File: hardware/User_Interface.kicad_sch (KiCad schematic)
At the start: 21 parts, among them J2 AYF531035, J3 Molex 5034800440, Q1 NMOS, Q2 NMOS

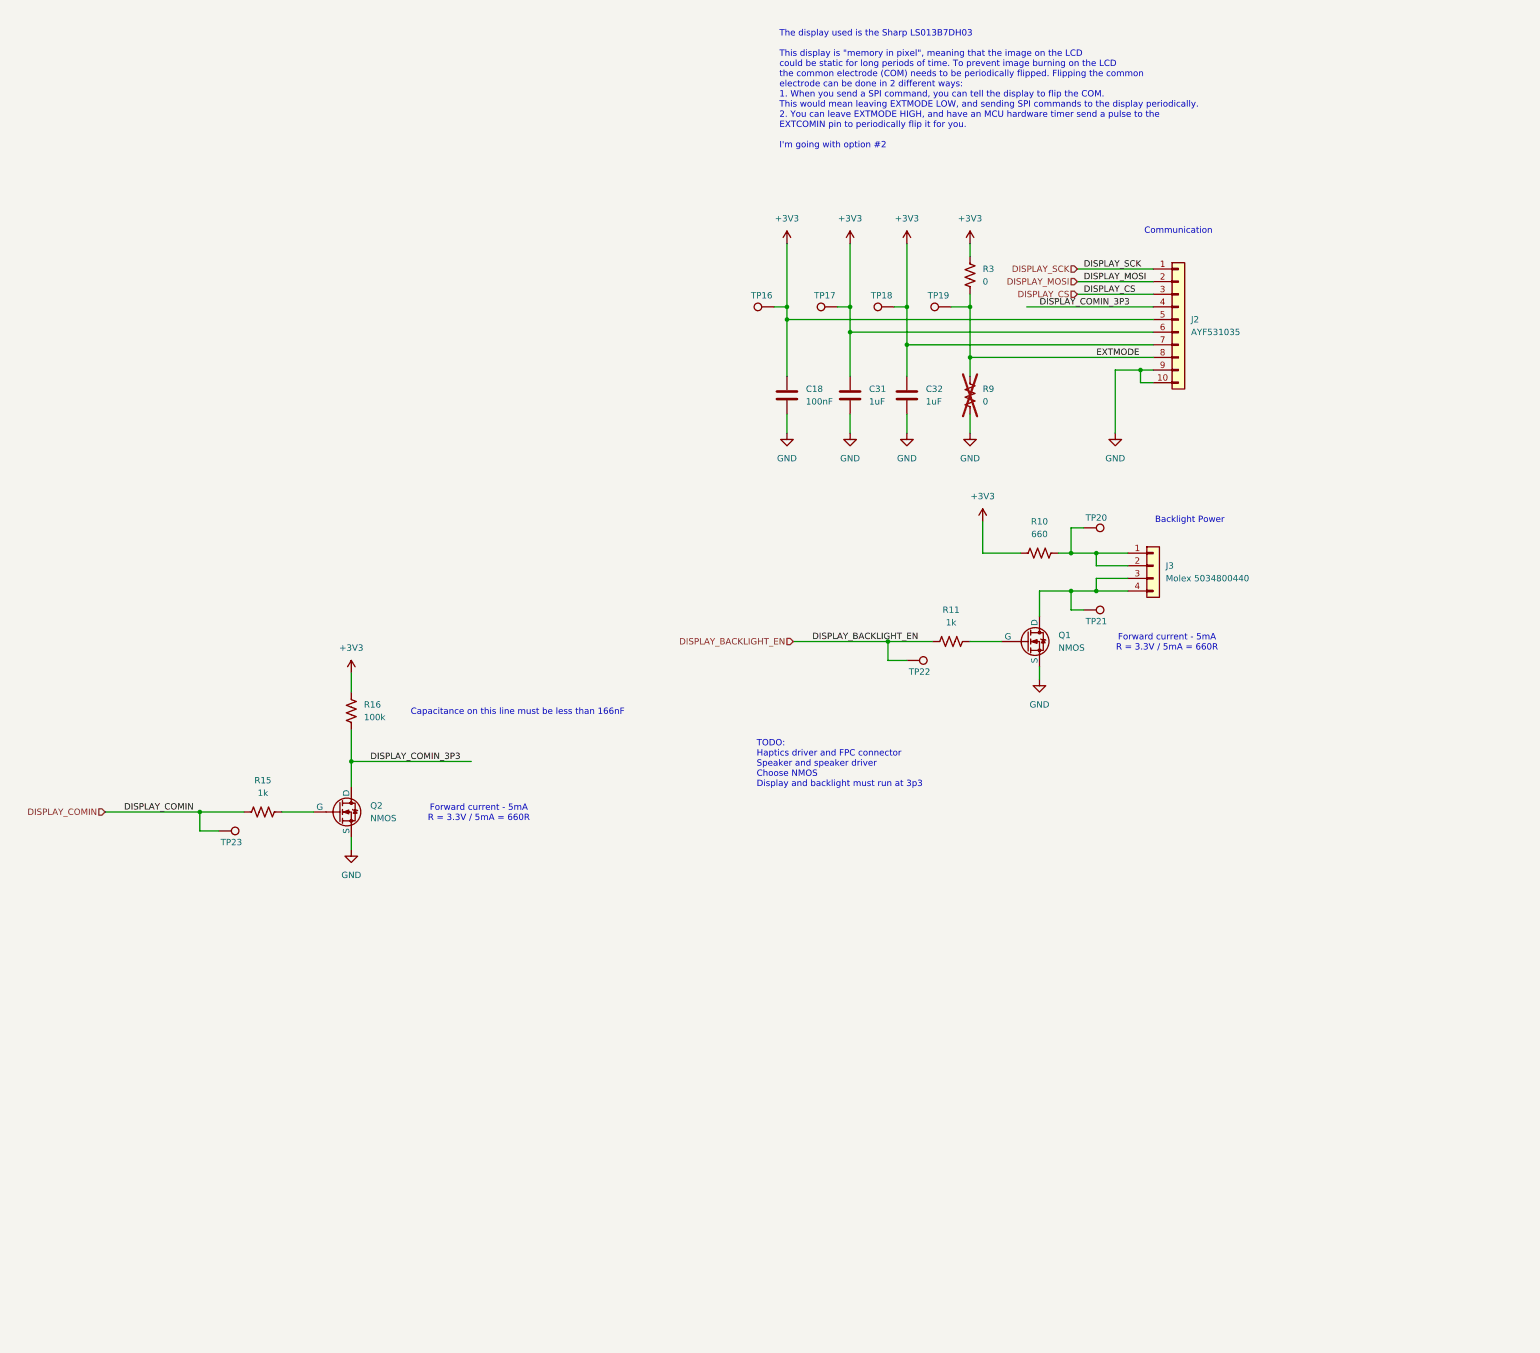
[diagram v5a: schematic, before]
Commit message: Added level translator, connected all misc GPIO. Ensured that 64QLFP has support for 1.8V
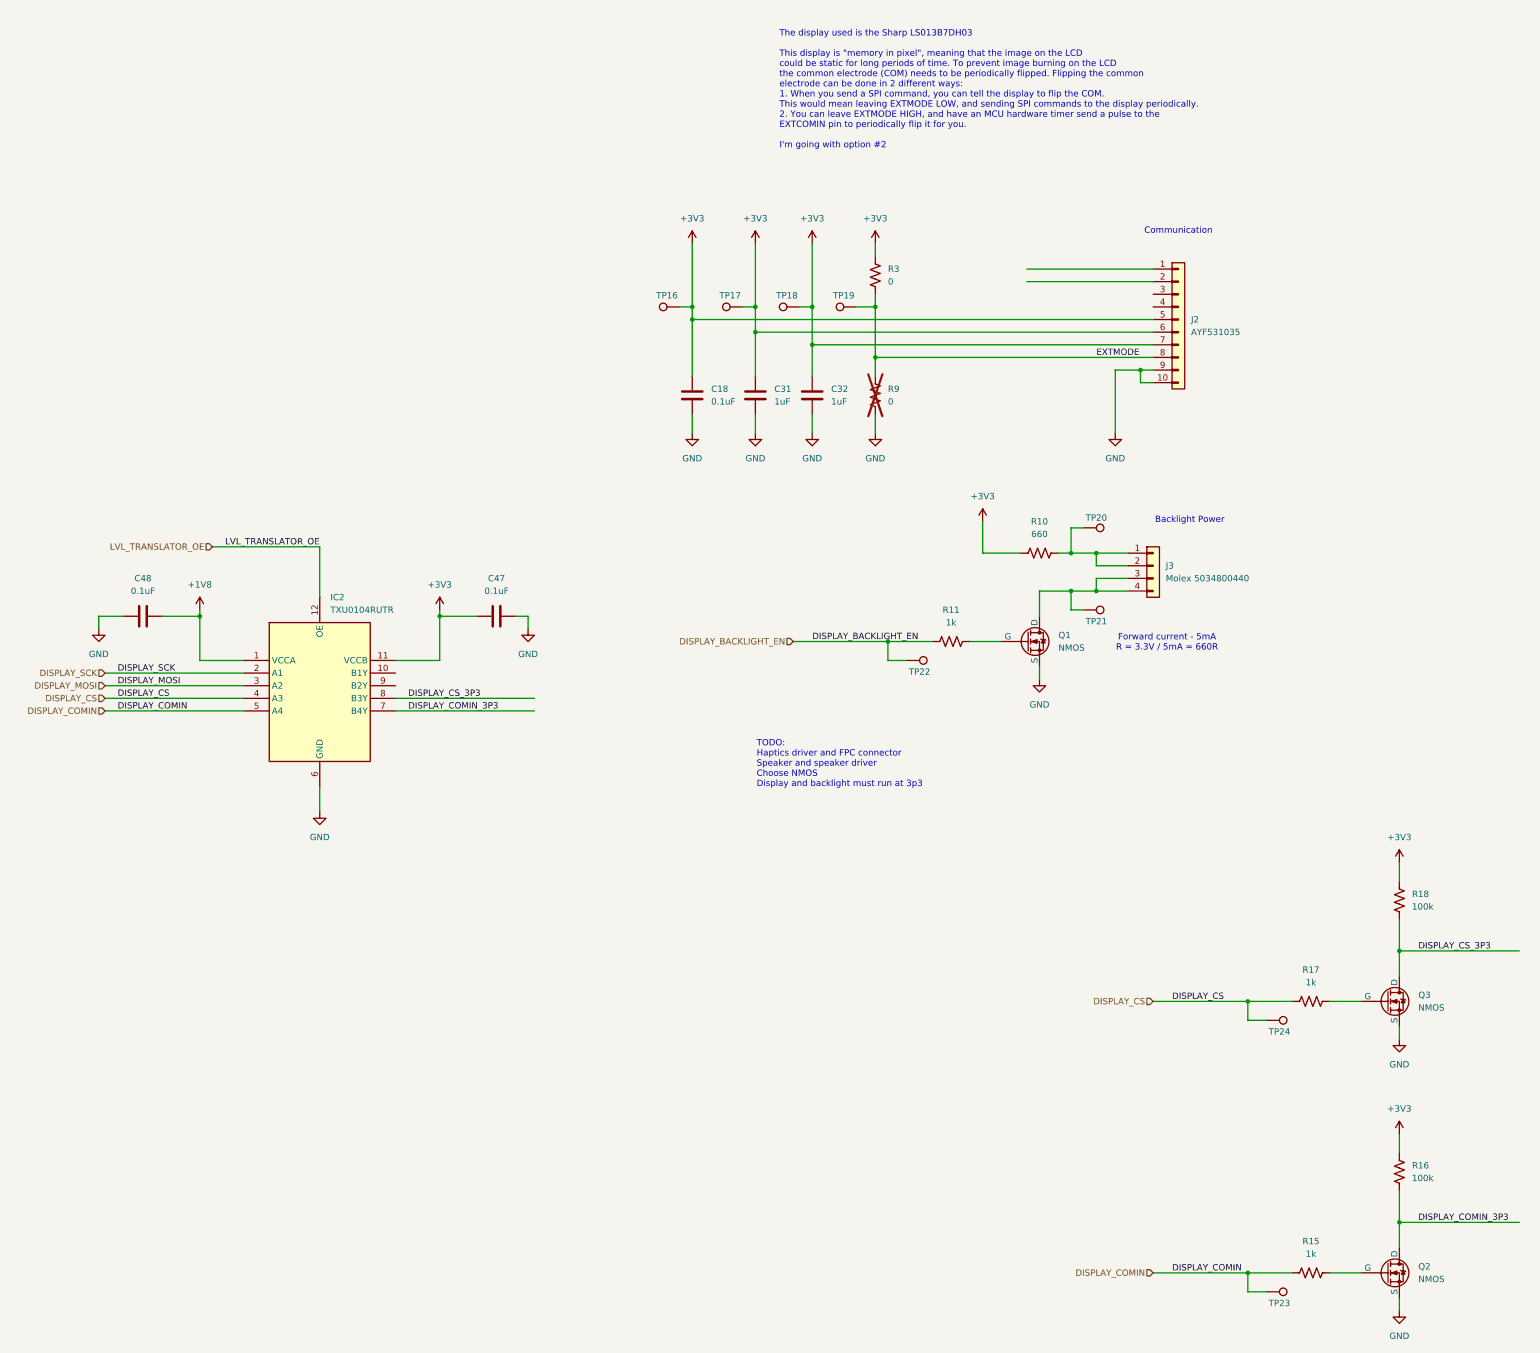
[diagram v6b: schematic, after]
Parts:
- added C47, C48: 0.1uF, symbol Device:C
- added IC2: TXU0104RUTR, TXU0104RUTR, symbol TXU0104RUTR:TXU0104RUTR
- added Q3: NMOS, symbol Simulation_SPICE:NMOS
- added R17: 1k, symbol Device:R_US
- added R18: 100k, symbol Device:R_US
- added TP24: TestPoint, symbol Connector:TestPoint
- C18: value 100nF -> 0.1uF
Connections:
- net +3V3: now also C47.1, IC2.11 (VCCB), R18.2
- net DISPLAY_COMIN: now also IC2.5 (A4)
- net DISPLAY_COMIN_3P3: now also IC2.7 (B4Y); no longer J2.4 (Pin_4)
- net DISPLAY_CS: now also IC2.4 (A3), R17.1, TP24.1; no longer J2.3 (Pin_3)
- net DISPLAY_MOSI: now also IC2.3 (A2); no longer J2.2 (Pin_2)
- net DISPLAY_SCK: now also IC2.2 (A1); no longer J2.1 (Pin_1)
- net GND: now also C47.2, C48.2, IC2.6 (GND), Q3.3 (S)
- new net: Q3.2 (G), R17.2
- new net +1V8: C48.1, IC2.1 (VCCA)
- new net DISPLAY_CS_3P3: IC2.8 (B3Y), Q3.1 (D), R18.1
- new net LVL_TRANSLATOR_OE: IC2.12 (OE)
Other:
- note removed: "Capacitance on this line must be less than 166nF"
- moved on the sheet: C18, C31, C32, Q2, R15, R16, R3, R9, TP16, TP17, TP18, TP19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
